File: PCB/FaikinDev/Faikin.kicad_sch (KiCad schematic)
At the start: 31 parts, among them J1 1x5, J2 TC2030-USB-NL, J3 Reset, Q1 BSS138PS, U1 TPS562243, U4 ESP32-S3-MINI-1

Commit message: Tweaks
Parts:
- added C1: 100nF, RevK:C_0201, symbol Device:C
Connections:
- net +3.3V: now also C1.2
- net GND: now also C1.1
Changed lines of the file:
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@@
 	)
 	(junction
+		(at 132.715 168.91)
+		(diameter 0)
+		(color 0 0 0 0)
+	)
+	(junction
 		(at 90.17 177.8)
 		(diameter 0)
@@
 	(wire
 		(pts
-			(xy 122.555 168.91) (xy 124.46 168.91)
+			(xy 122.555 168.91) (xy 132.715 168.91)
 		)
 		(stroke
@@
 	(wire
 		(pts
+			(xy 132.715 168.91) (xy 132.715 172.72)
+		)
+		(stroke
+			(width 0)
+			(type default)
+		)
+	)
+	(wire
+		(pts
 			(xy 43.815 165.735) (xy 43.815 168.91)
 		)
@@
 	(wire
 		(pts
+			(xy 132.715 168.91) (xy 136.525 168.91)
+		)
+		(stroke
+			(width 0)
+			(type default)
+		)
+	)
+	(wire
+		(pts
 			(xy 90.17 171.45) (xy 92.075 171.45)
 		)
@@
 	(wire
 		(pts
+			(xy 132.715 180.34) (xy 132.715 184.15)
+		)
+		(stroke
+			(width 0)
+			(type default)
+		)
+	)
+	(wire
+		(pts
 			(xy 92.075 166.37) (xy 92.075 168.91)
 		)
@@
 	(wire
 		(pts
+			(xy 132.715 184.15) (xy 122.555 184.15)
+		)
+		(stroke
+			(width 0)
+			(type default)
+		)
+	)
+	(wire
+		(pts
 			(xy 151.13 115.57) (xy 159.385 115.57)
 		)
@@
 	(symbol
 		(lib_id "power:+3.3V")
-		(at 124.46 168.91 270)
+		(at 136.525 168.91 270)
 		(unit 1)
 		(exclude_from_sim no)
@@
 		(dnp no)
 		(property "Reference" "#PWR029"
-			(at 120.65 168.91 0)
+			(at 132.715 168.91 0)
 			(effects
 				(font
@@
 		)
 		(property "Value" "+3.3V"
-			(at 124.333 166.878 90)
+			(at 136.398 166.878 90)
 			(effects
 				(font
@@
 		)
 		(property "Footprint" ""
-			(at 124.46 168.91 0)
+			(at 136.525 168.91 0)
 			(effects
 				(font
@@
 		)
 		(property "Datasheet" ""
-			(at 124.46 168.91 0)
+			(at 136.525 168.91 0)
 			(effects
 				(font
@@
 		)
 		(property "Description" "Power symbol creates a global label with name \"+3.3V\""
-			(at 124.46 168.91 0)
+			(at 136.525 168.91 0)
 			(effects
 				(font
@@
 					(unit 1)
 				)
+			)
+		)
+	)
+	(symbol
+		(lib_id "Device:C")
+		(at 132.715 176.53 180)
+		(unit 1)
+		(exclude_from_sim no)
+		(in_bom yes)
+		(on_board yes)
+		(dnp no)
+		(property "Reference" "C1"
+			(at 131.445 173.609 90)
+			(effects
+				(font
+					(size 1.27 1.27)
+				)
+			)
+		)
+		(property "Value" "100nF"
+			(at 134.239 172.212 90)
+			(effects
+				(font
+					(size 1.27 1.27)
+				)
+			)
+		)
+		(property "Footprint" "RevK:C_0201"
+			(at 131.7498 172.72 0)
+			(effects
+				(font
+					(size 1.27 1.27)
+				)
+				(hide yes)
+			)
+		)
+		(property "Datasheet" "~"
+			(at 132.715 176.53 0)
+			(effects
+				(font
+					(size 1.27 1.27)
+				)
+				(hide yes)
+			)
+		)
+		(property "Description" "Unpolarized capacitor"
+			(at 132.715 176.53 0)
+			(effects
+				(font
+					(size 1.27 1.27)
+				)
+				(hide yes)
+			)
+		)
+		(property "MPN" "C76934"
+			(at 132.715 176.53 90)
+			(effects
+				(font
+					(size 1.27 1.27)
+				)
+				(hide yes)
+			)
+		)
+		(pin "2"
+		)
+		(pin "1"
+		)
+		(instances
+			(project "Faikin"
+				(path "/46c350bb-7de4-4e81-aafd-4af55e37aab0"
+					(reference "C1")
+					(unit 1)
+				)

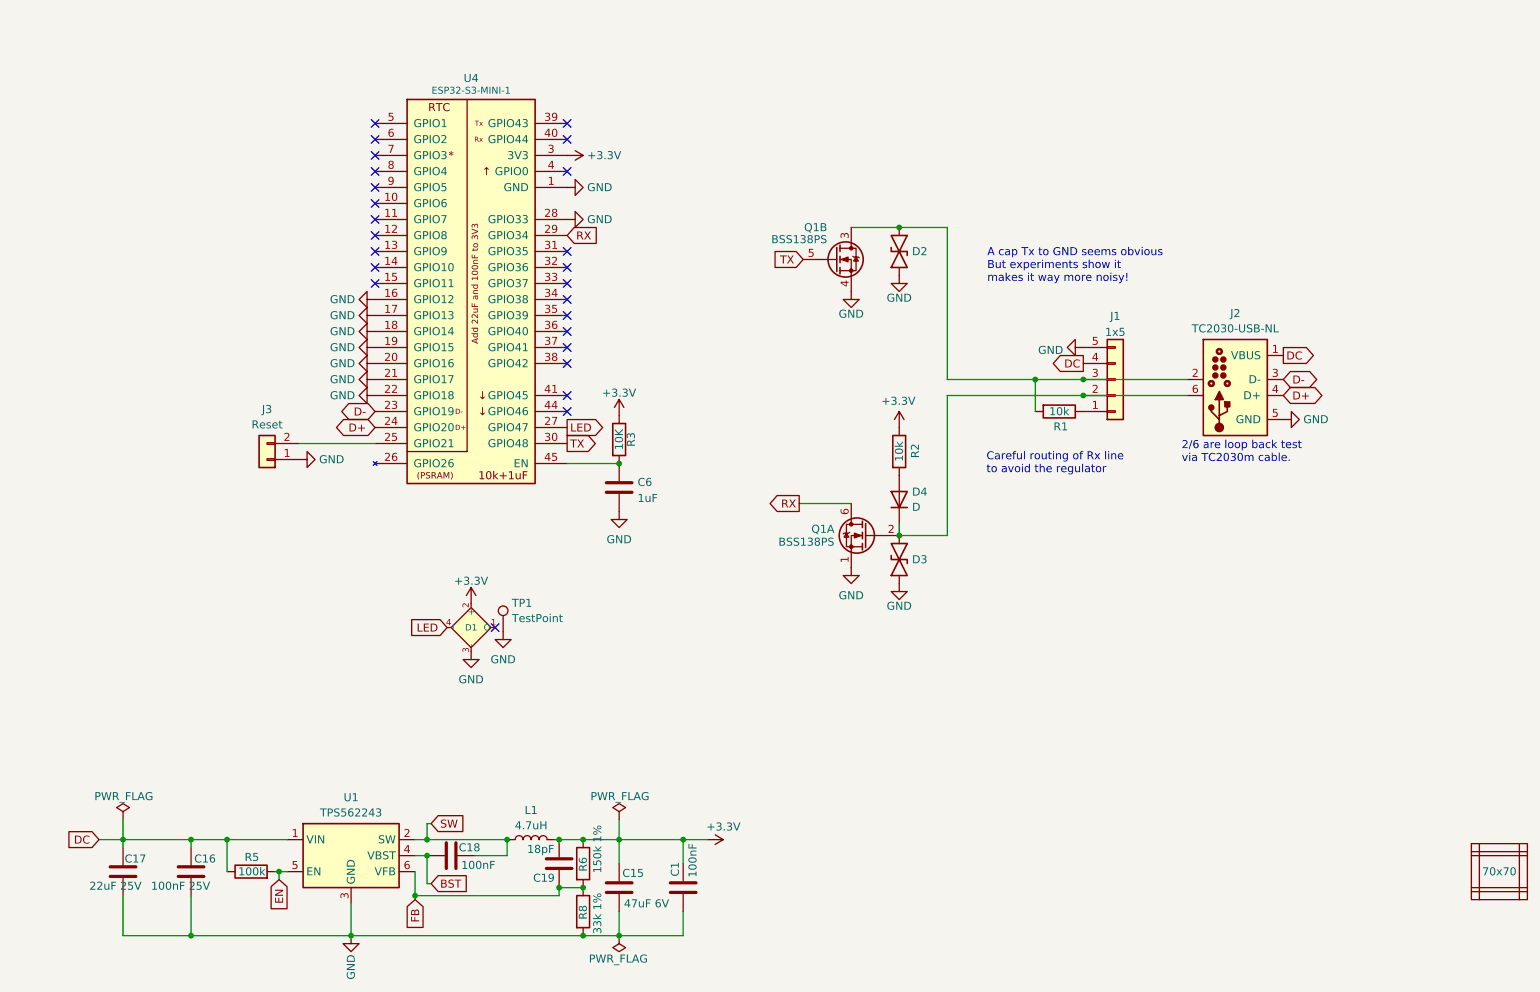
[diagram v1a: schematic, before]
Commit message: Moved caps away from heat
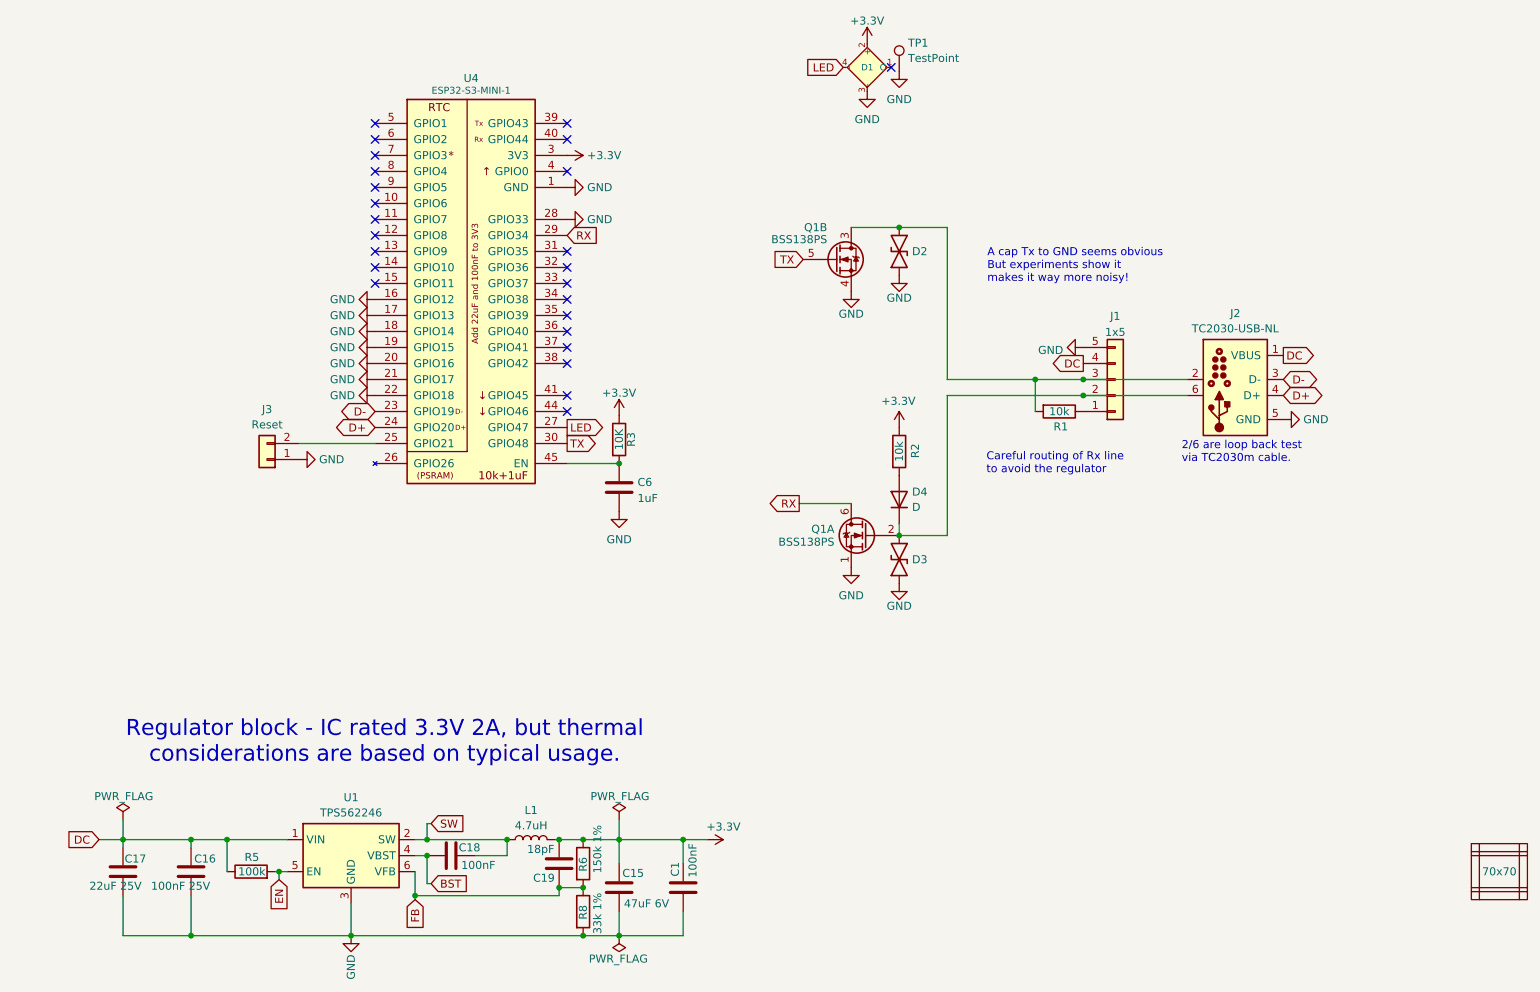
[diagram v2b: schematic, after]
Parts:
- U1: value TPS562243 -> TPS562246; symbol RevK:TPS562243 -> RevK:TPS562246; MPN C42295941 -> C41833479
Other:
- note added: "Regulator block - IC rated 3.3V 2A, but thermal considerations are based on typical usage."
- moved on the sheet: D1, TP1
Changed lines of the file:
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@@
 		)
 	)
+	(text "Regulator block - IC rated 3.3V 2A, but thermal\nconsiderations are based on typical usage."
+		(exclude_from_sim no)
+		(at 85.344 153.416 0)
+		(effects
+			(font
+				(size 2.54 2.54)
+			)
+		)
+	)
 	(junction
 		(at 113.03 176.53)
@@
 	)
 	(no_connect
-		(at 102.87 135.255)
+		(at 165.735 46.355)
 	)
 	(no_connect
@@
 	(global_label "LED"
 		(shape input)
-		(at 95.25 135.255 180)
+		(at 158.115 46.355 180)
 		(fields_autoplaced yes)
 		(effects
@@
 		)
 		(property "Intersheetrefs" "${INTERSHEET_REFS}"
-			(at 89.4719 135.255 0)
+			(at 152.3369 46.355 0)
 			(effects
 				(font
@@
 	(symbol
 		(lib_id "power:GND")
-		(at 99.06 139.065 0)
+		(at 161.925 50.165 0)
 		(unit 1)
 		(exclude_from_sim no)
@@
 		(fields_autoplaced yes)
 		(property "Reference" "#PWR023"
-			(at 99.06 145.415 0)
+			(at 161.925 56.515 0)
 			(effects
 				(font
@@
 		)
 		(property "Value" "GND"
-			(at 99.06 143.5084 0)
+			(at 161.925 54.6084 0)
 			(effects
 				(font
@@
 		)
 		(property "Footprint" ""
-			(at 99.06 139.065 0)
+			(at 161.925 50.165 0)
 			(effects
 				(font
@@
 		)
 		(property "Datasheet" ""
-			(at 99.06 139.065 0)
+			(at 161.925 50.165 0)
 			(effects
 				(font
@@
 		)
 		(property "Description" "Power symbol creates a global label with name \"GND\" , ground"
-			(at 99.06 139.065 0)
+			(at 161.925 50.165 0)
 			(effects
 				(font
@@
 	(symbol
 		(lib_id "Connector:TestPoint")
-		(at 104.14 135.89 0)
+		(at 167.005 46.99 0)
 		(unit 1)
 		(exclude_from_sim no)
@@
 		(fields_autoplaced yes)
 		(property "Reference" "TP1"
-			(at 105.537 131.3758 0)
+			(at 168.402 42.4758 0)
 			(effects
 				(font
@@
 		)
 		(property "Value" "TestPoint"
-			(at 105.537 133.8001 0)
+			(at 168.402 44.9001 0)
 			(effects
 				(font
@@
 		)
 		(property "Footprint" "RevK:1x2-Hole"
-			(at 109.22 135.89 0)
+			(at 172.085 46.99 0)
 			(effects
 				(font
@@
 		)
 		(property "Datasheet" "~"
-			(at 109.22 135.89 0)
+			(at 172.085 46.99 0)
 			(effects
 				(font
@@
 		)
 		(property "Description" "test point"
-			(at 104.14 135.89 0)
+			(at 167.005 46.99 0)
 			(effects
 				(font
@@
 	(symbol
 		(lib_id "power:GND")
-		(at 104.14 135.89 0)
+		(at 167.005 46.99 0)
 		(unit 1)
 		(exclude_from_sim no)
@@
 		(fields_autoplaced yes)
 		(property "Reference" "#PWR027"
-			(at 104.14 142.24 0)
+			(at 167.005 53.34 0)
 			(effects
 				(font
@@
 		)
 		(property "Value" "GND"
-			(at 104.14 140.3334 0)
+			(at 167.005 51.4334 0)
 			(effects
 				(font
@@
 		)
 		(property "Footprint" ""
-			(at 104.14 135.89 0)
+			(at 167.005 46.99 0)
 			(effects
 				(font
@@
 		)
 		(property "Datasheet" ""
-			(at 104.14 135.89 0)
+			(at 167.005 46.99 0)
 			(effects
 				(font
@@
 		)
 		(property "Description" "Power symbol creates a global label with name \"GND\" , ground"
-			(at 104.14 135.89 0)
+			(at 167.005 46.99 0)
 			(effects
 				(font
@@
 	)
 	(symbol
-		(lib_id "RevK:TPS562243")
+		(lib_id "RevK:TPS562246")
 		(at 80.01 171.45 0)
 		(unit 1)
@@
 			)
 		)
-		(property "Value" "TPS562243"
+		(property "Value" "TPS562246"
 			(at 80.01 164.6498 0)
 			(effects
@@
 			)
 		)
-		(property "Datasheet" "https://www.ti.com/lit/gpn/tps562243"
+		(property "Datasheet" "https://www.ti.com/lit/ds/symlink/tps562246.pdf"
 			(at 80.01 171.45 0)
 			(effects
@@
 			)
 		)
-		(property "MPN" "C42295941"
+		(property "MPN" "C41833479"
 			(at 80.01 171.45 0)
 			(effects
@@
 	(symbol
 		(lib_id "power:+3.3V")
-		(at 99.06 131.445 0)
+		(at 161.925 42.545 0)
 		(unit 1)
 		(exclude_from_sim no)
@@
 		(fields_autoplaced yes)
 		(property "Reference" "#PWR022"
-			(at 99.06 135.255 0)
+			(at 161.925 46.355 0)
 			(effects
 				(font
@@
 		)
 		(property "Value" "+3.3V"
-			(at 99.06 127.8692 0)
+			(at 161.925 38.9692 0)
 			(effects
 				(font
@@
 		)
 		(property "Footprint" ""
-			(at 99.06 131.445 0)
+			(at 161.925 42.545 0)
 			(effects
 				(font
@@
 		)
 		(property "Datasheet" ""
-			(at 99.06 131.445 0)
+			(at 161.925 42.545 0)
 			(effects
 				(font
@@
 		)
 		(property "Description" "Power symbol creates a global label with name \"+3.3V\""
-			(at 99.06 131.445 0)
+			(at 161.925 42.545 0)
 			(effects
 				(font
@@
 	(symbol
 		(lib_id "RevK:WS2812B-1mm")
-		(at 99.06 135.255 0)
+		(at 161.925 46.355 0)
 		(mirror x)
 		(unit 1)
@@
 		(dnp no)
 		(property "Reference" "D1"
-			(at 99.06 135.255 0)
+			(at 161.925 46.355 0)
 			(do_not_autoplace yes)
 			(effects
@@
 		)
 		(property "Value" "XL-1010RGBC-WS2812B"
-			(at 100.33 129.54 0)
+			(at 163.195 40.64 0)
 			(effects
 				(font
@@
 		)
 		(property "Footprint" "RevK:SMD1010"
-			(at 100.33 127.635 0)
+			(at 163.195 38.735 0)
 			(effects
 				(font
@@
 		)
 		(property "Datasheet" "https://datasheet.lcsc.com/lcsc/2301111010_XINGLIGHT-XL-1010RGBC-WS2812B_C5349953.pdf"
-			(at 100.33 125.73 0)
+			(at 163.195 36.83 0)
 			(effects
 				(font
@@
 		)
 		(property "Description" "RGB LED with integrated controller"
-			(at 99.06 135.255 0)
+			(at 161.925 46.355 0)
 			(effects
 				(font
@@
 		)
 		(property "MPN" "C5349953"
-			(at 100.33 123.825 0)
+			(at 163.195 34.925 0)
 			(effects
 				(font

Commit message: PCB tweak
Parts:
- added C2, C3, C4: 100nF, RevK:C_0201, symbol Device:C
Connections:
- net +3.3V: now also C2.2, C3.2, C4.2
- net GND: now also C2.1, C3.1, C4.1

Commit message: Tweaks
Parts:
- U1: Rotation Offset -90 -> 180
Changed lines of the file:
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@@
 			)
 		)
-		(property "Rotation Offset" "-90"
+		(property "Rotation Offset" "180"
 			(at 80.01 171.45 0)
 			(effects

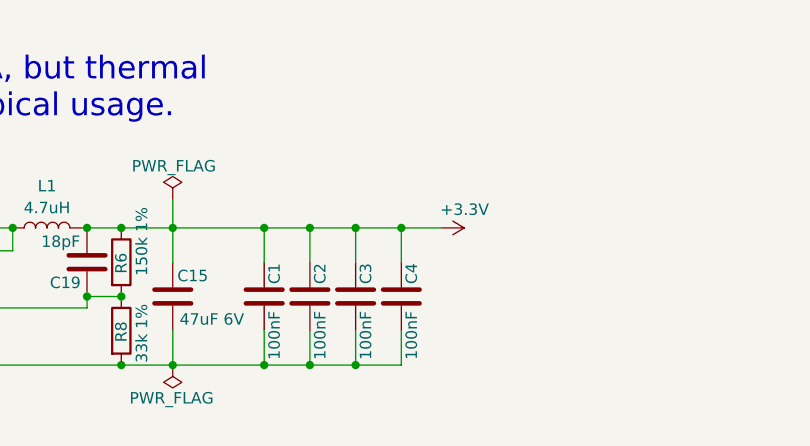
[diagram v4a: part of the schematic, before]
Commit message: Tweak caps and inductor
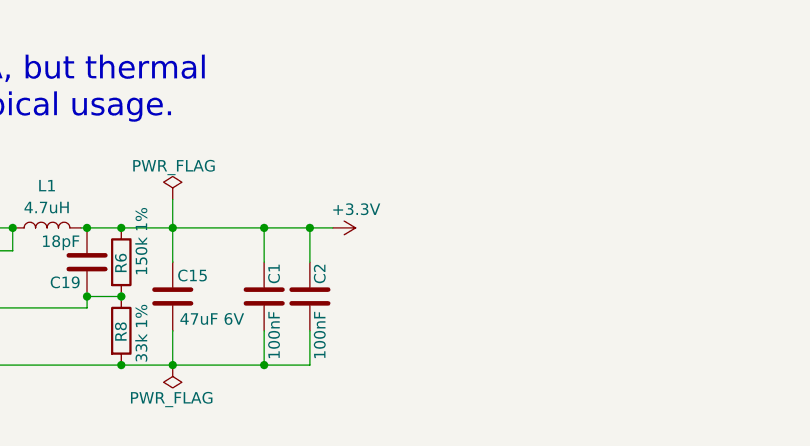
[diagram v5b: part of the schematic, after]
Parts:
- removed C3, C4: 100nF, RevK:C_0201, symbol Device:C

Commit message: You can never have too many caps.
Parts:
- added C3: 100nF 25V, RevK:C_0402, symbol Device:C
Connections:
- net DC: now also C3.1
- net GND: now also C3.2
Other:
- moved on the sheet: C17
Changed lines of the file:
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@@
 	)
 	(junction
+		(at 46.355 184.15)
+		(diameter 0)
+		(color 0 0 0 0)
+	)
+	(junction
 		(at 122.555 109.22)
 		(diameter 0)
@@
 	)
 	(junction
-		(at 43.815 168.91)
+		(at 46.355 168.91)
+		(diameter 0)
+		(color 0 0 0 0)
+	)
+	(junction
+		(at 36.195 168.91)
 		(diameter 0)
 		(color 0 0 0 0)
@@
 	(wire
 		(pts
+			(xy 46.355 184.15) (xy 36.195 184.15)
+		)
+		(stroke
+			(width 0)
+			(type default)
+		)
+	)
+	(wire
+		(pts
 			(xy 54.61 177.8) (xy 54.61 184.15)
 		)
@@
 	(wire
 		(pts
-			(xy 43.815 165.735) (xy 43.815 168.91)
+			(xy 36.195 165.735) (xy 36.195 168.91)
+		)
+		(stroke
+			(width 0)
+			(type default)
+		)
+	)
+	(wire
+		(pts
+			(xy 46.355 177.8) (xy 46.355 184.15)
 		)
 		(stroke
@@
 	(wire
 		(pts
+			(xy 46.355 168.91) (xy 46.355 170.18)
+		)
+		(stroke
+			(width 0)
+			(type default)
+		)
+	)
+	(wire
+		(pts
 			(xy 54.61 168.91) (xy 60.325 168.91)
 		)
@@
 	(wire
 		(pts
-			(xy 43.815 184.15) (xy 43.815 177.8)
+			(xy 36.195 184.15) (xy 36.195 177.8)
 		)
 		(stroke
@@
 	(wire
 		(pts
-			(xy 54.61 184.15) (xy 43.815 184.15)
+			(xy 54.61 184.15) (xy 46.355 184.15)
+		)
+		(stroke
+			(width 0)
+			(type default)
+		)
+	)
+	(wire
+		(pts
+			(xy 36.195 168.91) (xy 36.195 170.18)
 		)
 		(stroke
@@
 	(wire
 		(pts
-			(xy 43.815 168.91) (xy 43.815 170.18)
+			(xy 46.355 168.91) (xy 54.61 168.91)
 		)
 		(stroke
@@
 	(wire
 		(pts
-			(xy 40.005 168.91) (xy 43.815 168.91)
+			(xy 32.385 168.91) (xy 36.195 168.91)
 		)
 		(stroke
@@
 	(wire
 		(pts
-			(xy 43.815 168.91) (xy 54.61 168.91)
+			(xy 36.195 168.91) (xy 46.355 168.91)
 		)
 		(stroke
@@
 	(global_label "DC"
 		(shape input)
-		(at 40.005 168.91 180)
+		(at 32.385 168.91 180)
 		(fields_autoplaced yes)
 		(effects
@@
 		)
 		(property "Intersheetrefs" "${INTERSHEET_REFS}"
-			(at 35.134 168.91 0)
+			(at 27.514 168.91 0)
 			(effects
 				(font
@@
 	)
 	(symbol
+		(lib_id "Device:C")
+		(at 46.355 173.99 0)
+		(unit 1)
+		(exclude_from_sim no)
+		(in_bom yes)
+		(on_board yes)
+		(dnp no)
+		(property "Reference" "C3"
+			(at 47.498 177.8 90)
+			(effects
+				(font
+					(size 1.27 1.27)
+				)
+				(justify left)
+			)
+		)
+		(property "Value" "100nF 25V"
+			(at 43.18 182.88 90)
+			(effects
+				(font
+					(size 1.27 1.27)
+				)
+				(justify left)
+			)
+		)
+		(property "Footprint" "RevK:C_0402"
+			(at 47.3202 177.8 0)
+			(effects
+				(font
+					(size 1.27 1.27)
+				)
+				(hide yes)
+			)
+		)
+		(property "Datasheet" "~"
+			(at 46.355 173.99 0)
+			(effects
+				(font
+					(size 1.27 1.27)
+				)
+				(hide yes)
+			)
+		)
+		(property "Description" "Unpolarized capacitor"
+			(at 46.355 173.99 0)
+			(effects
+				(font
+					(size 1.27 1.27)
+				)
+				(hide yes)
+			)
+		)
+		(property "MPN" "C56392"
+			(at 46.355 173.99 0)
+			(effects
+				(font
+					(size 1.27 1.27)
+				)
+				(hide yes)
+			)
+		)
+		(pin "2"
+		)
+		(pin "1"
+		)
+		(instances
+			(project "Faikin"
+				(path "/46c350bb-7de4-4e81-aafd-4af55e37aab0"
+					(reference "C3")
+					(unit 1)
+				)
+			)
+		)
+	)
+	(symbol
 		(lib_id "power:GND")
 		(at 161.925 50.165 0)
@@
 		(dnp no)
 		(property "Reference" "C16"
-			(at 55.118 171.958 0)
+			(at 55.626 179.07 90)
 			(effects
 				(font
@@
 		)
 		(property "Value" "100nF 25V"
-			(at 48.26 176.276 0)
+			(at 51.308 182.88 90)
 			(effects
 				(font
@@
 	(symbol
 		(lib_id "power:PWR_FLAG")
-		(at 43.815 165.735 0)
+		(at 36.195 165.735 0)
 		(unit 1)
 		(exclude_from_sim no)
@@
 		(dnp no)
 		(property "Reference" "#FLG01"
-			(at 43.815 163.83 0)
+			(at 36.195 163.83 0)
 			(effects
 				(font
@@
 		)
 		(property "Value" "PWR_FLAG"
-			(at 43.942 162.052 0)
+			(at 36.322 162.052 0)
 			(effects
 				(font
@@
 		)
 		(property "Footprint" ""
-			(at 43.815 165.735 0)
+			(at 36.195 165.735 0)
 			(effects
 				(font
@@
 		)
 		(property "Datasheet" "~"
-			(at 43.815 165.735 0)
+			(at 36.195 165.735 0)
 			(effects
 				(font
@@
 		)
 		(property "Description" "Special symbol for telling ERC where power comes from"
-			(at 43.815 165.735 0)
+			(at 36.195 165.735 0)
 			(effects
 				(font
@@
 	(symbol
 		(lib_id "Device:C")
-		(at 43.815 173.99 0)
+		(at 36.195 173.99 0)
 		(unit 1)
 		(exclude_from_sim no)
@@
 		(dnp no)
 		(property "Reference" "C17"
-			(at 44.069 171.958 0)
+			(at 37.338 179.07 90)
 			(effects
 				(font
@@
 		)
 		(property "Value" "22uF 25V"
-			(at 38.481 176.276 0)
+			(at 33.02 182.88 90)
 			(effects
 				(font
@@
 		)
 		(property "Footprint" "RevK:C_0805"
-			(at 44.7802 177.8 0)
+			(at 37.1602 177.8 0)
 			(effects
 				(font
@@
 		)
 		(property "Datasheet" "~"
-			(at 43.815 173.99 0)
+			(at 36.195 173.99 0)
 			(effects
 				(font
@@
 		)
 		(property "Description" "Unpolarized capacitor"
-			(at 43.815 173.99 0)
+			(at 36.195 173.99 0)
 			(effects
 				(font
@@
 		)
 		(property "MPN" "C45783"
-			(at 43.815 173.99 0)
+			(at 36.195 173.99 0)
 			(effects
 				(font

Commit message: FFS
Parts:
- added C4, C5: 100nF, RevK:C_0201, symbol Device:C
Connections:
- net +3.3V: now also C4.2, C5.2
- net GND: now also C4.1, C5.1
